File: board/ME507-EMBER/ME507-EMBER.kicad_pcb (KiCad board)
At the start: 2 copper layers, 20 parts, among them J1 Screw_Terminal_01x02, J2 Screw_Terminal_01x04, J3 Screw_Terminal_01x02, J4 Screw_Terminal_01x04, J5 Screw_Terminal_01x08, Q1 Q_NMOS_GDS, U1 DRV8871DDA, U2 DRV8871DDA

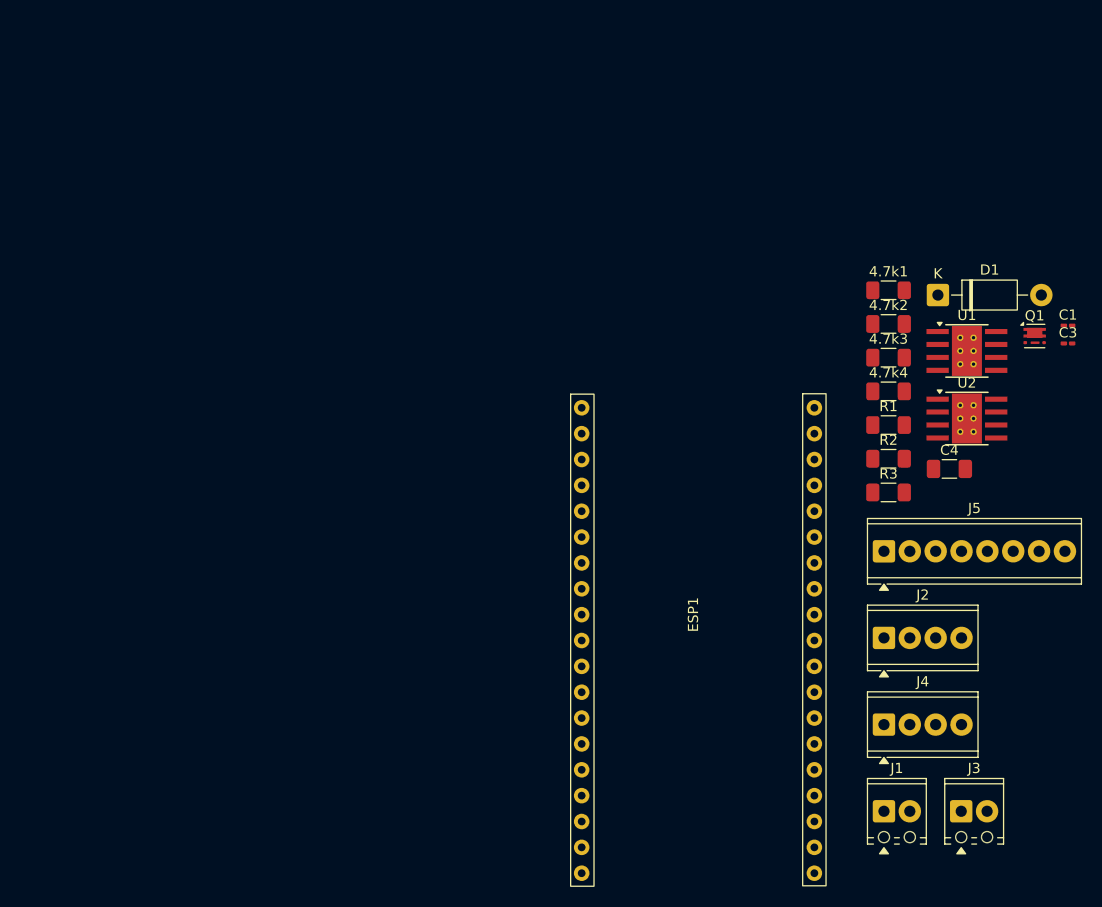
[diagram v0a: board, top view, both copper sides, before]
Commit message: new file:   board/ME507-EMBER/EMBER_Footprints.pretty/EMBER_Vishay_PowerPAK_1212-8.kicad_mod 	new file:   board/ME507-EMBER/EMBER_Footprints.pretty/MOSFET_Vishay_PowerPAK_1212-8_Single_JACKSON.kicad_mod 	new file:   board/ME507-EMBER/ME507-EMBER-backups/ME507-EMBER-2025-10-24_173205.zip 	new file:   board/ME507-EMBER/ME507-EMBER-backups/ME507-EMBER-2025-10-24_174214.zip 	new file:   board/ME507-EMBER/ME507-EMBER-backups/ME507-EMBER-2025-10-24_174817.zip 	new file:   board/ME507-EMBER/ME507-EMBER-backups/ME507-EMBER-2025-10-24_175957.zip 	new file:   board/ME507-EMBER/ME507-EMBER-backups/ME507-EMBER-2025-10-24_180838.zip 	modified:   board/ME507-EMBER/ME507-EMBER.kicad_pcb 	modified:   board/ME507-EMBER/ME507-EMBER.kicad_prl 	modified:   board/ME507-EMBER/ME507-EMBER.kicad_pro 	modified:   board/ME507-EMBER/ME507-EMBER.kicad_sch 	modified:   board/ME507-EMBER/fp-info-cache 	new file:   board/ME507-EMBER/fp-lib-table
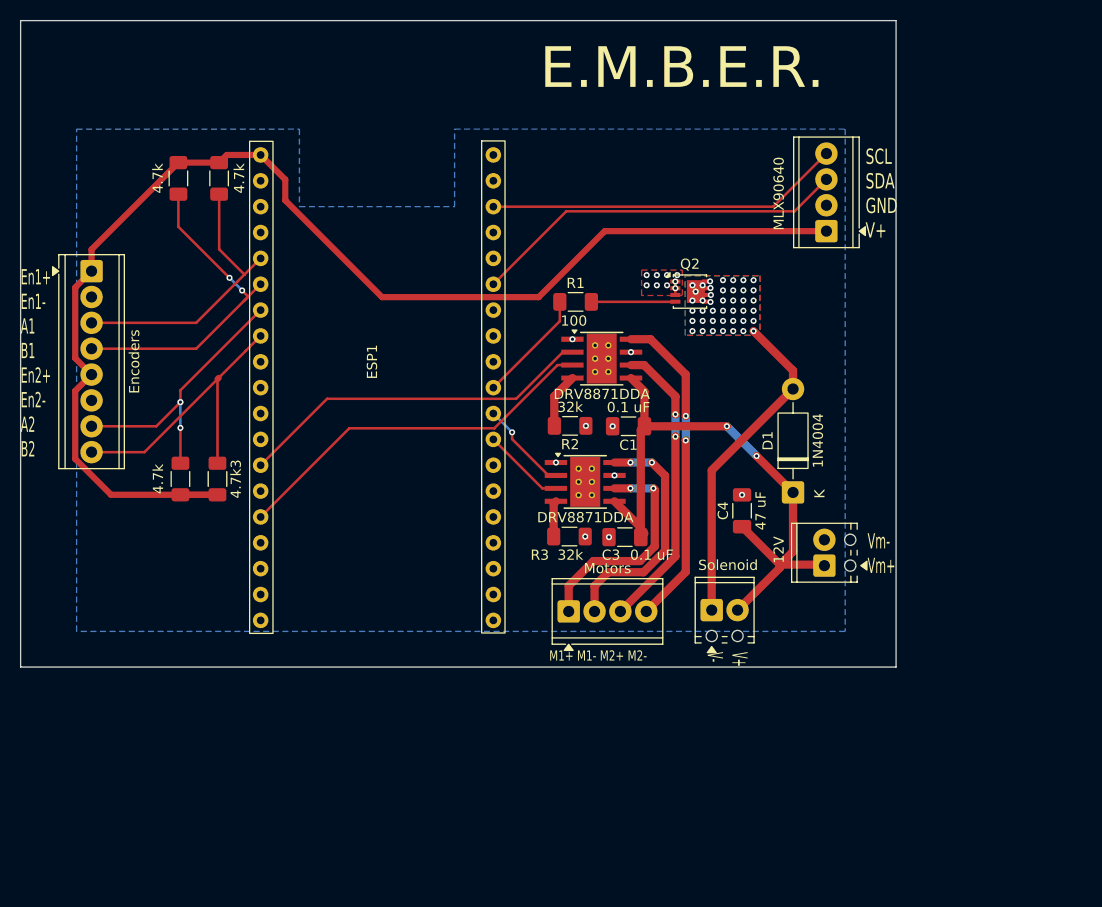
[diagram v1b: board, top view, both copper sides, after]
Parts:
- removed Q1: Q_NMOS_GDS, Package_TO_SOT_SMD:Vishay_PowerPAK_SC70-6L_Single
- added Q2: Q_NMOS_SGD, EMBER_Footprints:MOSFET_Vishay_PowerPAK_1212-8_Single_JACKSON, F.Cu at (95.3, 54.1)
- 12V: renamed from J3; value Screw_Terminal_01x02 -> External Power (12V)
- C1, C3: footprint Capacitor_SMD:C_0201_0603Metric_Pad0.64x0.40mm_HandSolder -> Capacitor_SMD:C_1206_3216Metric_Pad1.33x1.80mm_HandSolder
- Encoders: renamed from J5; value Screw_Terminal_01x08 -> Encoder Terminal
- MLX90640: renamed from J2; value Screw_Terminal_01x04 -> IR Cam Terminal
- Motors: renamed from J4; value Screw_Terminal_01x04 -> DC Motor Terminal
- Solenoid: renamed from J1; value Screw_Terminal_01x02 -> Solenoid Terminal
- moved Encoders 82.6 mm to (36.5, 52.1), turned to -90 degrees
- moved 4.7k 71.2 mm to (45.2, 72.5), turned to -90 degrees
- moved 4.7k 70.6 mm to (45.0, 43.0), turned to 90 degrees
- moved 4.7k 69.0 mm to (49.0, 43.0), turned to 90 degrees
- moved 4.7k3 67.0 mm to (48.8, 72.5), turned to -90 degrees
- moved C3 47.5 mm to (88.9, 78.2), turned to 180 degrees
- moved C1 44.3 mm to (89.2, 67.3), turned to 180 degrees
- moved MLX90640 40.4 mm to (108.7, 48.2), turned to 90 degrees
- moved ESP1 40.1 mm to (64.5, 61.0)
- moved U1 39.6 mm to (85.0, 72.8)
- moved U2 36.4 mm to (86.6, 60.7)
- moved R1 33.0 mm to (84.0, 55.1)
- moved Motors 32.9 mm to (83.3, 85.5)
- moved R3 31.6 mm to (83.4, 78.2), turned to 180 degrees
- moved R2 31.4 mm to (83.5, 67.3), turned to 180 degrees
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- renumbered 4.7k2 to 4.7k, 4.7k1 to 4.7k, 4.7k4 to 4.7k
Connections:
- D1 pad 2: Net-(D1-A) -> /Q_D
- Solenoid pad 1: /Vm -> /Q_D
- Solenoid pad 2: Net-(D1-A) -> /Vm
- U1 pad 2: Net-(ESP1-GPIO16/RX2) -> Net-(ESP1-GPIO17/TX2)
- U1 pad 3: Net-(ESP1-GPIO17/TX2) -> Net-(ESP1-GPIO16/RX2)
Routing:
- net +3V3: track 0.00 -> 128.4 mm
- net /Vm: track 0.00 -> 61.7 mm, vias 0 -> 2
- net Net-(ESP1-GPIO21/SDA): track 0.00 -> 37.0 mm
- net Net-(ESP1-GPIO13): track 0.00 -> 36.8 mm
- net Net-(ESP1-GPIO12): track 0.00 -> 35.2 mm
- net Net-(ESP1-GPIO22/SCL): track 0.00 -> 34.9 mm
- net Net-(ESP1-GPI35/ADC7): track 0.00 -> 32.8 mm, vias 0 -> 2
- net /Q_D: track 0.00 -> 32.3 mm, vias 0 -> 42
- net Net-(J4-Pin_4): track 0.00 -> 31.7 mm, vias 0 -> 2
- net Net-(ESP1-GPIO33/ADC5): track 0.00 -> 29.8 mm
- net Net-(J4-Pin_3): track 0.00 -> 29.0 mm, vias 0 -> 2
- net Net-(ESP1-GPI34/ADC6): track 0.00 -> 28.2 mm
- net Net-(ESP1-GPIO32/ADC4): track 0.00 -> 28.0 mm, vias 0 -> 2
- net Net-(J4-Pin_2): track 0.00 -> 23.7 mm, vias 0 -> 2
- net Net-(J4-Pin_1): track 0.00 -> 22.1 mm, vias 0 -> 2
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- added copper zone on B.Cu, net /Q_D
- added copper zone on F.Cu, net /Q_D
- added copper zone on B.Cu, net GND
- added copper zone on F.Cu, net GND
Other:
- board outline added: 86 x 63.5 mm
- board text added: "4.7k"
- board text added: "E.M.B.E.R."
- board text added: "En1+ En1- A1 B1 En2+ En2- A2 B2"
- board text added: "M1+ M1- M2+ M2-"
- board text added: "SCL SDA GND V+"
- board text added: "V+ V-"
- board text added: "Vm- Vm+"

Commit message: deleted:    board/ME507-EMBER/ME507-EMBER-backups/ME507-EMBER-2025-10-24_173205.zip 	new file:   board/ME507-EMBER/ME507-EMBER-backups/ME507-EMBER-2025-10-24_181717.zip 	new file:   board/ME507-EMBER/ME507-EMBER-backups/ME507-EMBER-2025-10-27_165905.zip 	new file:   board/ME507-EMBER/ME507-EMBER-backups/ME507-EMBER-2025-10-27_170905.zip 	new file:   board/ME507-EMBER/ME507-EMBER-backups/ME507-EMBER-2025-10-27_172403.zip 	new file:   board/ME507-EMBER/ME507-EMBER-backups/ME507-EMBER-2025-10-27_173500.zip 	new file:   board/ME507-EMBER/ME507-EMBER-backups/ME507-EMBER-2025-10-27_174108.zip 	modified:   board/ME507-EMBER/ME507-EMBER.kicad_pcb 	modified:   board/ME507-EMBER/ME507-EMBER.kicad_sch
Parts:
- added H1: MountingHole, MountingHole:MountingHole_2.7mm_M2.5, F.Cu at (41.0, 31.0)
- added H2: MountingHole, MountingHole:MountingHole_2.7mm_M2.5, F.Cu at (113.0, 31.0)
- added H3: MountingHole, MountingHole:MountingHole_2.7mm_M2.5, F.Cu at (41.0, 87.0)
- added H4: MountingHole, MountingHole:MountingHole_2.7mm_M2.5, F.Cu at (113.0, 87.0)
- added J6: IMU Terminal, TerminalBlock_Phoenix:TerminalBlock_Phoenix_MPT-0,5-4-2.54_1x04_P2.54mm_Horizontal, F.Cu at (108.8, 61.0)
- added R5: ~, Resistor_SMD:R_1206_3216Metric_Pad1.30x1.75mm_HandSolder, F.Cu at (94.6, 48.5)
- added R6: ~, Resistor_SMD:R_1206_3216Metric_Pad1.30x1.75mm_HandSolder, F.Cu at (99.8, 48.6)
- J1: renamed from Solenoid; value Solenoid Terminal -> Solenoid
- U1, U2: value DRV8871DDA -> DRV8871
- moved J1 20.6 mm to (108.8, 68.2), turned to 90 degrees
- moved U2 15.7 mm to (93.9, 74.6), turned to -90 degrees
- moved C3 10.4 mm to (78.7, 76.3), turned to 90 degrees
- moved R8 9.14 mm to (78.5, 70.5), turned to -90 degrees
- moved J5 9.09 mm to (45.2, 49.7)
- moved C1 8.89 mm to (89.4, 76.2), turned to 90 degrees
- moved D1 7.95 mm to (102.7, 66.4), turned to 180 degrees
- moved C4 7.13 mm to (101.8, 82.6), turned to -90 degrees
- moved R9 6.88 mm to (89.6, 70.5), turned to -90 degrees
- moved Q2 6.52 mm to (91.3, 59.3)
- moved U1 2.83 mm to (82.8, 74.6), turned to -90 degrees
- moved J2 0.68 mm to (108.7, 48.9)
- renumbered ESP1 to ESP32, MLX90640 to J2, 12V to J3, Motors to J4, Encoders to J5, 4.7k to R1, 4.7k to R2, 4.7k to R3, 4.7k3 to R4, R1 to R7, R3 to R8, R2 to R9
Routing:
- net Net-(J4-Pin_4): track 31.7 -> 10.1 mm
- net Net-(J4-Pin_3): track 29.0 -> 10.0 mm
- net Net-(ESP32-GPIO21/SDA): track 37.0 -> 53.8 mm, vias 0 -> 1
- net Net-(ESP32-GPIO22/SCL): track 34.9 -> 50.9 mm, vias 0 -> 2
- net Net-(J4-Pin_2): track 23.7 -> 8.68 mm
- net Net-(J4-Pin_1): track 22.1 -> 8.63 mm
- net /Q_D: track 32.3 -> 19.0 mm, vias 42 -> 40
- net Net-(ESP32-GPIO12): track 35.2 -> 48.1 mm, vias 0 -> 2
- net Net-(ESP32-GPIO13): track 36.8 -> 48.4 mm
- net Net-(ESP32-GPI35/ADC7): track 32.8 -> 21.2 mm
- net Net-(ESP32-GPI34/ADC6): track 28.2 -> 17.0 mm
- net /Vm: track 61.7 -> 71.3 mm, vias 2 -> 0
- net +3V3: track 128.4 -> 132.5 mm
- net Net-(ESP32-GPIO32/ADC4): track 28.0 -> 24.4 mm
- net Net-(ESP32-GPIO33/ADC5): track 29.8 -> 26.3 mm
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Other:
- board size 86 x 63.5 mm -> 79.2 x 63.5 mm

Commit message: new file:   board/ME507-EMBER/ME507-EMBER-backups/ME507-EMBER-2025-10-30_154305.zip 	new file:   board/ME507-EMBER/ME507-EMBER-backups/ME507-EMBER-2025-10-30_160009.zip 	new file:   board/ME507-EMBER/ME507-EMBER-backups/ME507-EMBER-2025-10-30_160613.zip 	new file:   board/ME507-EMBER/ME507-EMBER-backups/ME507-EMBER-2025-10-30_161352.zip 	new file:   board/ME507-EMBER/ME507-EMBER-backups/ME507-EMBER-2025-10-30_162427.zip 	modified:   board/ME507-EMBER/ME507-EMBER.kicad_pcb 	modified:   board/ME507-EMBER/ME507-EMBER.kicad_prl 	modified:   board/ME507-EMBER/ME507-EMBER.kicad_sch
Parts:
- removed Q2: Q_NMOS_SGD, EMBER_Footprints:MOSFET_Vishay_PowerPAK_1212-8_Single_JACKSON
- added Q1: SVD5867NLT4G, Package_TO_SOT_SMD:TO-252-2, F.Cu at (93.7, 56.4)
- R5, R6: value ~ -> 4.7k
- moved J4 4.22 mm to (87.6, 85.6)
- moved U1 1.82 mm to (84.6, 74.5)
- moved U2 1.82 mm to (95.7, 74.5)
- moved R8 1.26 mm to (79.7, 70.9)
- moved R7 1.13 mm to (84.0, 54.0)
- moved C3 1.08 mm to (79.7, 76.4)
- moved R9 0.93 mm to (90.5, 70.5)
- moved C1 0.93 mm to (90.4, 76.3)
- moved R5 0.82 mm to (93.7, 48.6)
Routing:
- net Net-(Q1-G): track 9.03 -> 3.21 mm
- net Net-(ESP32-GPIO12): track 48.1 -> 49.9 mm
- net Net-(ESP32-GPIO17/TX2): track 10.3 -> 12.0 mm
- net Net-(ESP32-GPIO16/RX2): track 8.70 -> 10.4 mm
- net Net-(ESP32-GPIO13): track 48.4 -> 49.9 mm
- net Net-(ESP32-GPIO5): track 11.1 -> 12.6 mm
- net /Q_D: track 19.0 -> 17.7 mm, vias 40 -> 45
- net GND: track 1.32 -> 0.00 mm, vias 18 -> 21
- net Net-(J4-Pin_1): track 8.63 -> 9.77 mm
- net Net-(J4-Pin_2): track 8.68 -> 9.74 mm
- net /Vm: track 71.3 -> 70.3 mm
- net Net-(U2-ILIM): track 2.49 -> 3.45 mm
- net Net-(U1-ILIM): track 2.44 -> 3.33 mm
- net Net-(J4-Pin_4): track 10.1 -> 9.21 mm
- net Net-(J4-Pin_3): track 10.0 -> 9.20 mm
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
